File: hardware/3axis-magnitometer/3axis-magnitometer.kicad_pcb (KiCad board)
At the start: 2 copper layers, 94 x 94 mm, 84 parts, among them J1 Conn_01x40_Pin, J2 AVR-JTAG-10, J3 AVR-ISP-6, U1 PCF8563T, U10 SP3485CN, U11 LSM6DS3, U2 W25Q128JVS, U3 ATmega1284P-A, U4 QMC5883P, U5 AMS1117-3.3, U6 AMS1117-3.3, U7 74LVC2T45DC, U8 74LVC2T45DC, U9 SP3485CN, Y1 32.768кГц, Y2 8MHz

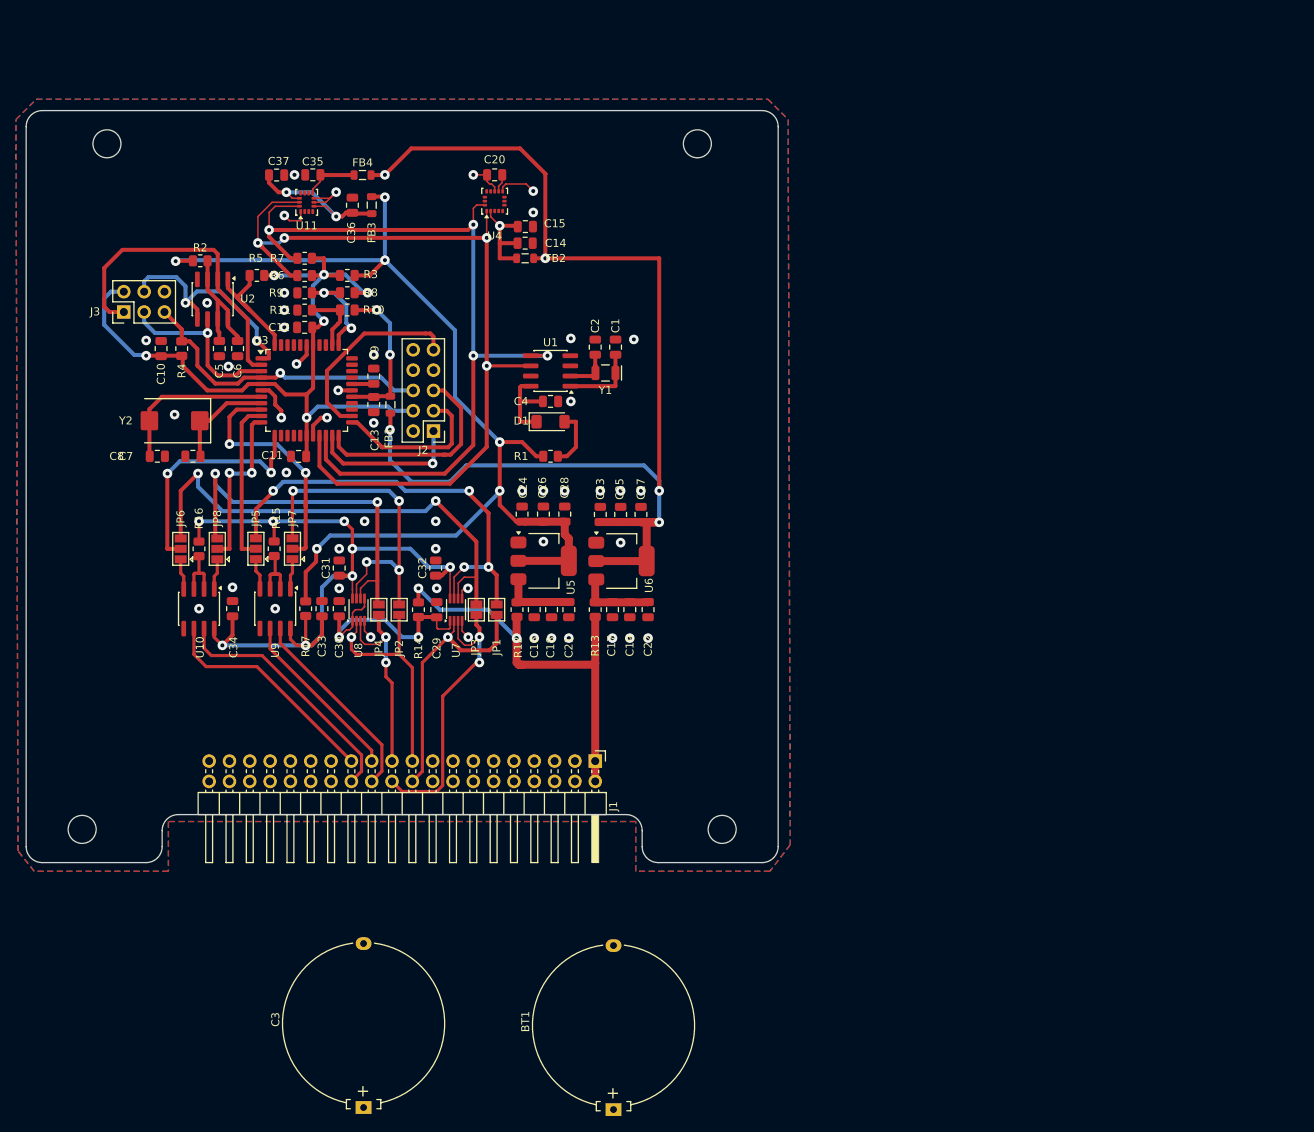
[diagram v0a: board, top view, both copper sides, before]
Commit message: Магнитометр правки
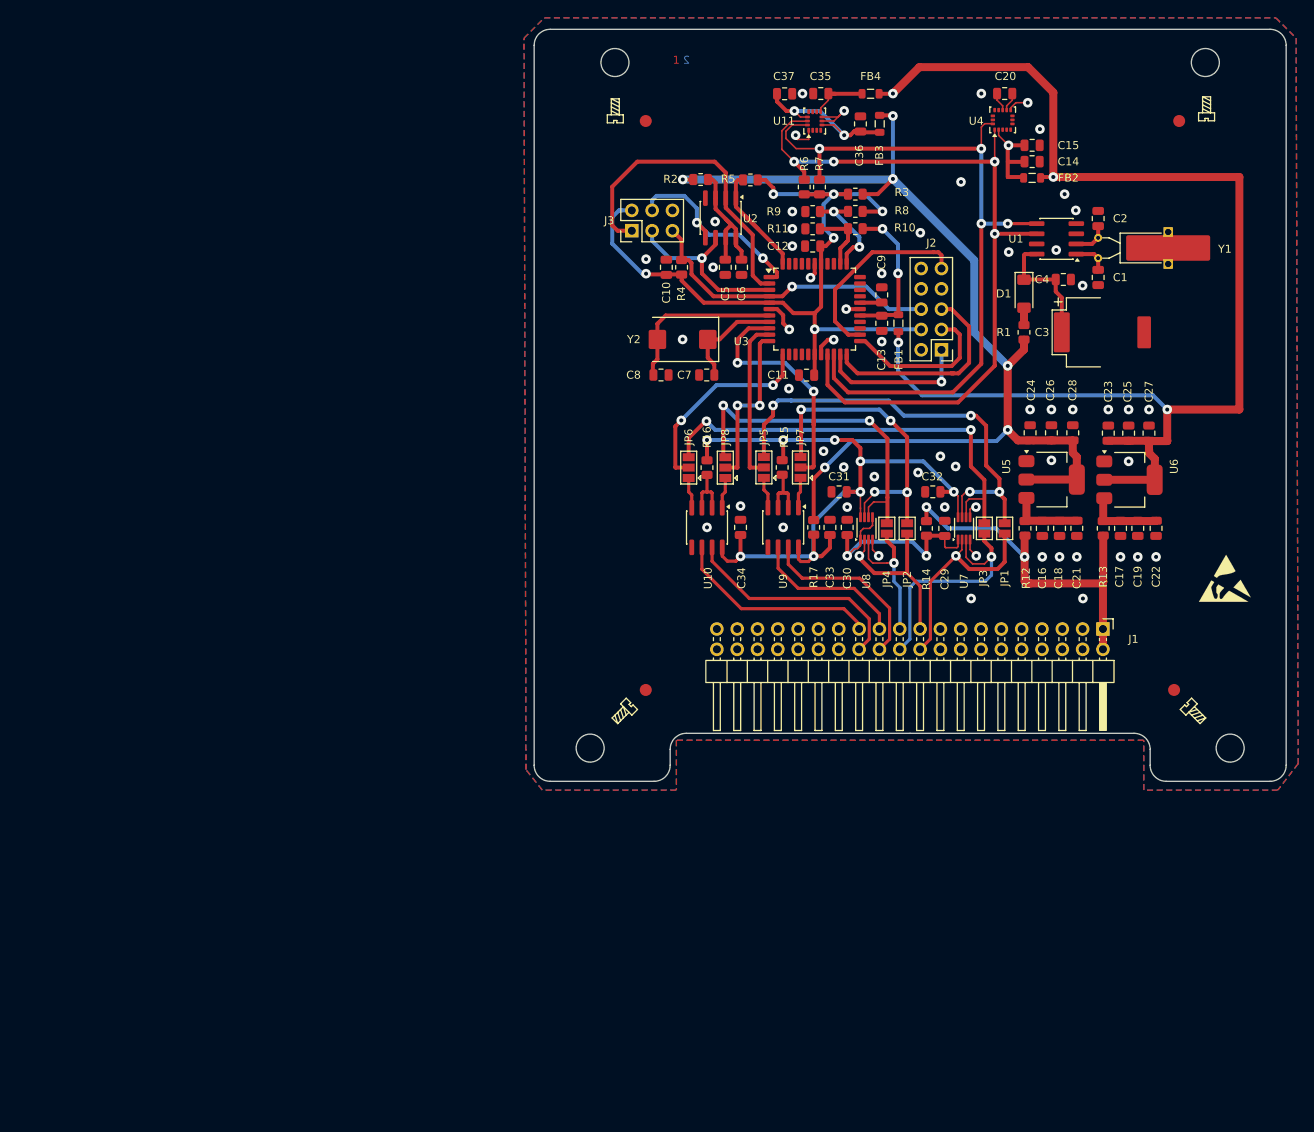
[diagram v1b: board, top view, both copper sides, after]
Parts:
- removed BT1: Battery_Cell, Battery:Battery_Panasonic_CR2032-HFN_Horizontal_CircularHoles
- added REF**: LayerMarker_2_3.81x2.54mm_TextH1mm_P1.27mm_BottomMirrored, Symbol:LayerMarker_2_3.81x2.54mm_TextH1mm_P1.27mm_BottomMirrored, F.Cu at (107.5, 43.8)
- added REF**: Screw_Generic_2.0x3.0mm_SilkScreen, Symbol:Screw_Generic_2.0x3.0mm_SilkScreen, F.Cu at (173.8, 48.7)
- added REF**: Fiducial_1.5mm_Mask3mm, Fiducial:Fiducial_1.5mm_Mask3mm, F.Cu at (103.7, 121.3)
- added REF**: Screw_Generic_2.0x3.0mm_SilkScreen, Symbol:Screw_Generic_2.0x3.0mm_SilkScreen, F.Cu at (172.3, 124.1)
- added REF**: Screw_Generic_2.0x3.0mm_SilkScreen, Symbol:Screw_Generic_2.0x3.0mm_SilkScreen, F.Cu at (100.9, 124.1)
- added REF**: Fiducial_1.5mm_Mask3mm, Fiducial:Fiducial_1.5mm_Mask3mm, F.Cu at (169.8, 121.3)
- added REF**: ESD-Logo_6.6x6mm_SilkScreen, Symbol:ESD-Logo_6.6x6mm_SilkScreen, F.Cu at (176.1, 107.3)
- added REF**: Screw_Generic_2.0x3.0mm_SilkScreen, Symbol:Screw_Generic_2.0x3.0mm_SilkScreen, F.Cu at (99.9, 48.9)
- added REF**: Fiducial_1.5mm_Mask3mm, Fiducial:Fiducial_1.5mm_Mask3mm, F.Cu at (170.4, 50.2)
- added REF**: Fiducial_1.5mm_Mask3mm, Fiducial:Fiducial_1.5mm_Mask3mm, F.Cu at (103.7, 50.2)
- C3: footprint Battery:Battery_Panasonic_CR2032-HFN_Horizontal_CircularHoles -> IONISTOR:DSK
- Y1: footprint Crystal:Crystal_SMD_EuroQuartz_EQ161-2Pin_3.2x1.5mm -> Crystal:Crystal_AT310_D3.0mm_L10.0mm_Horizontal_1EP_style2
- moved C3 133.9 mm to (160.9, 76.6), turned to 0 degrees
- moved C4 65.9 mm to (155.9, 70.0)
- moved J1 65.6 mm to (160.9, 113.7)
- moved U1 65.4 mm to (155.1, 64.9)
- moved C7 65.0 mm to (111.3, 81.9)
- moved R7 65.0 mm to (125.4, 58.4), turned to 90 degrees
- moved C2 64.9 mm to (160.3, 62.4)
- moved C20 64.6 mm to (148.6, 46.8)
- moved FB1 64.3 mm to (135.3, 75.5)
- moved C19 64.3 mm to (165.2, 101.1)
- moved C21 64.3 mm to (157.6, 101.1)
- moved C25 64.3 mm to (164.1, 89.2)
- moved C30 64.3 mm to (128.9, 101.0)
- moved C33 64.3 mm to (126.7, 101.0)
- moved C35 64.3 mm to (125.6, 46.8)
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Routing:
- net +3.3VA: track 147.5 -> 163.6 mm, vias 5 -> 4
- net /SDA: track 103.8 -> 94.5 mm
- net /SCL: track 107.2 -> 98.4 mm
- net /level_translator/RX0: track 28.9 -> 21.9 mm
- net /level_translator/RX1: track 25.1 -> 18.4 mm, vias 2 -> 1
- net Net-(D1-K): track 10.6 -> 17.1 mm
- net GND: track 39.6 -> 33.2 mm, vias 49 -> 57
- net +5V: track 53.4 -> 47.1 mm
- net /level_translator/TX0: track 32.9 -> 26.6 mm
- net Net-(U10-VCC): track 96.8 -> 91.1 mm
- net /level_translator/TX1: track 36.4 -> 30.8 mm, vias 2 -> 1
- net Net-(JP3-B): track 62.0 -> 56.3 mm
- net Net-(D1-A): track 7.34 -> 1.91 mm
- net Net-(U1-OSCI): track 9.66 -> 4.71 mm
- net /level_translator/UART_TX1: track 30.4 -> 25.9 mm
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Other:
- outline, holes or cut-outs redrawn

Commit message: Финальные правки трассировки
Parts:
- added C3: C_Polarized, IONISTOR:DSK, F.Cu at (170.4, 76.2)
- moved C23 8.60 mm to (176.1, 101.1)
- moved C18 8.60 mm to (171.7, 101.1)
- moved C20 8.60 mm to (173.8, 101.1)
- moved C24 8.60 mm to (170.1, 89.2)
- moved C26 8.60 mm to (172.7, 89.2)
- moved C28 8.60 mm to (175.2, 89.2)
- moved R13 8.60 mm to (169.5, 101.1)
- moved U6 8.60 mm to (172.8, 95.0)
- moved REF** 7.01 mm to (176.7, 114.3)
- moved C17 3.44 mm to (156.7, 101.1)
- moved C19 3.44 mm to (158.9, 101.1)
- moved C25 3.44 mm to (155.2, 89.2)
- moved C27 3.44 mm to (157.9, 89.2)
- moved C22 3.44 mm to (161.0, 101.1)
- moved C29 3.44 mm to (160.5, 89.2)
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- renumbered C9 to C10, C10 to C11, C11 to C12, C12 to C13, C13 to C14, C14 to C15, C15 to C16, C16 to C17, C17 to C18, C18 to C19, C19 to C20, C20 to C21, C21 to C22, C22 to C23, C23 to C24, C24 to C25, C25 to C26, C26 to C27, C27 to C28, C28 to C29, C29 to C30, C30 to C31, C31 to C32, C32 to C33, C33 to C34, C34 to C35, C35 to C36, C36 to C37, C37 to C38, C3 to C4, C4 to C5, C5 to C6, C6 to C7, C7 to C8, C8 to C9
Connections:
- Y1 pad 3: (no net) -> GND
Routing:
- net Net-(D1-K): track 17.1 -> 31.2 mm
- net +5V: track 47.1 -> 53.5 mm
- net +3.3VA: track 163.6 -> 158.8 mm
- net +3.3V: track 135.0 -> 137.1 mm
- net Net-(U10-VCC): track 91.1 -> 90.2 mm
- net GND: vias 57 -> 56

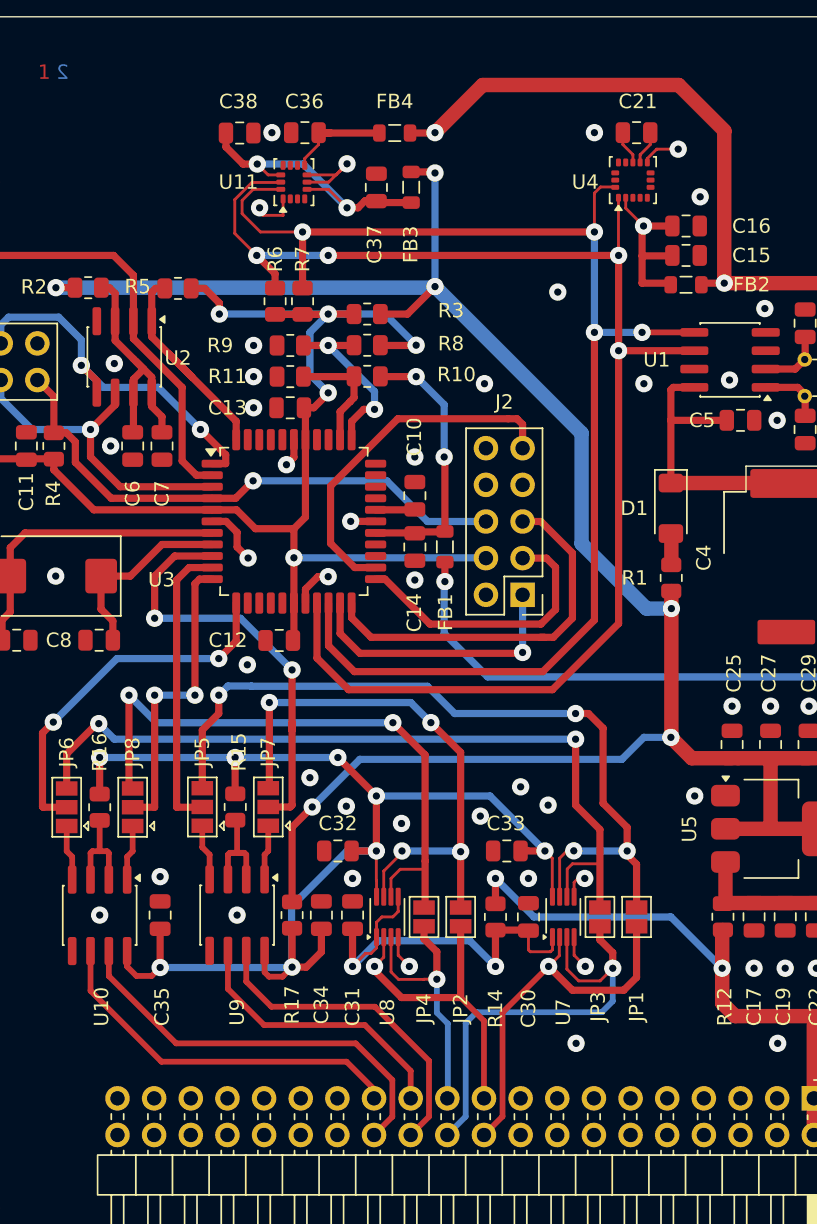
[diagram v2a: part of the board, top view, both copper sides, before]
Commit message: замена микросхемы преобразователя  уровня
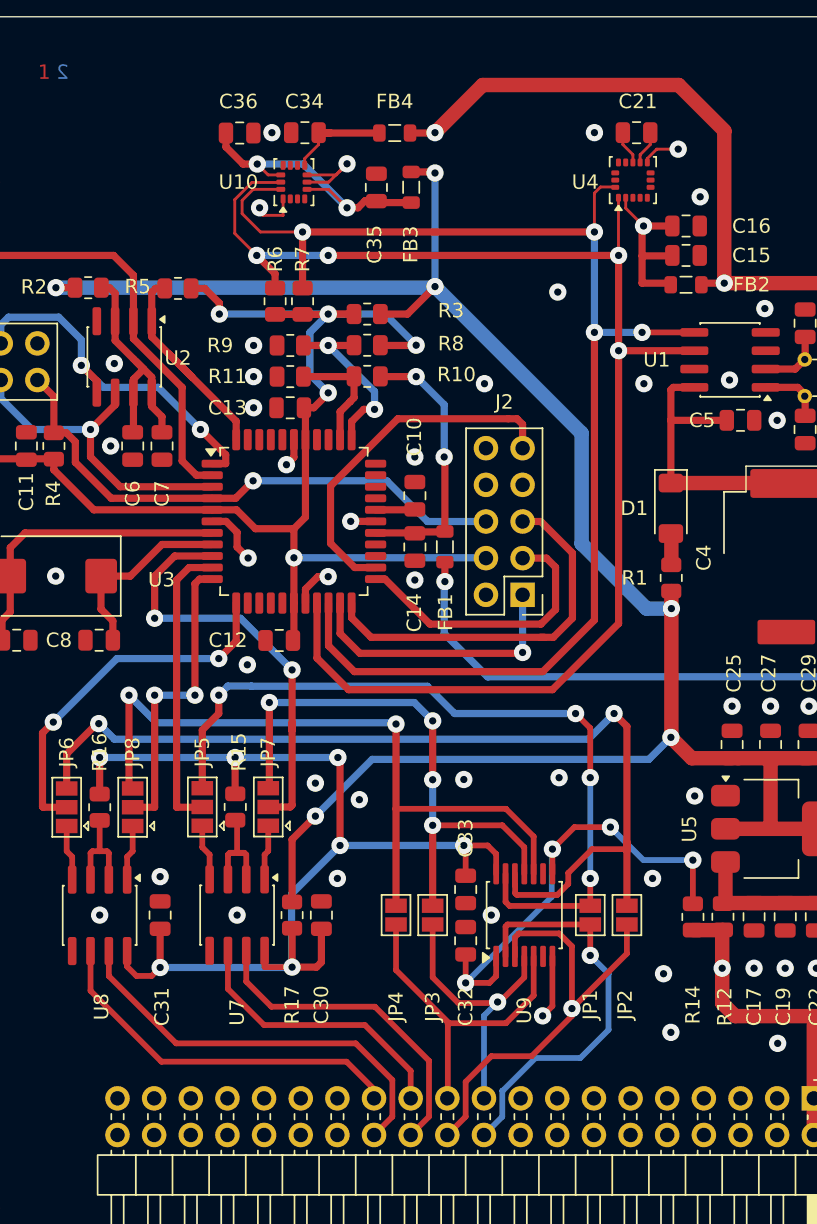
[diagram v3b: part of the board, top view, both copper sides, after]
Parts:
- removed the C30 at (141.1, 101.1)
- removed the C31 at (128.9, 101.0)
- removed the C33 at (139.6, 96.5)
- removed the U7 at (143.5, 101.1)
- removed the U8 at (131.3, 101.1)
- added C32: 0.22, Capacitor_SMD:C_0805_2012Metric, F.Cu at (136.7, 102.8)
- added U9: TXB0104PW, Package_SO:TSSOP-14_4.4x5mm_P0.65mm, F.Cu at (140.8, 101.0)
- moved R14 13.7 mm to (152.5, 101.1), turned to 90 degrees
- moved C33 9.25 mm to (136.7, 99.2), turned to -90 degrees
- moved JP1 3.21 mm to (145.4, 101.0)
- moved JP4 1.94 mm to (131.9, 101.0)
- moved JP3 1.94 mm to (134.5, 101.0)
- moved JP2 1.87 mm to (147.9, 101.0)
- renumbered C34 to C30, C35 to C31, C32 to C33, C36 to C34, C37 to C35, C38 to C36, JP3 to JP2, JP2 to JP3, U11 to U10, U9 to U7, U10 to U8
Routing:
- net +5V: track 53.5 -> 35.5 mm, vias 2 -> 1
- net Net-(U7-VCC): track 90.2 -> 78.2 mm, vias 8 -> 7
- net Net-(JP2-B): track 56.3 -> 68.0 mm
- net Net-(JP4-B): track 43.9 -> 51.4 mm
- net /level_translator/RX1: track 18.4 -> 23.1 mm, vias 1 -> 0
- net Net-(U9-OE): track 29.6 -> 33.5 mm, vias 2 -> 4
- net /level_translator/TX0: track 26.6 -> 28.5 mm
- net GND: track 33.2 -> 31.3 mm, vias 56 -> 54
- net /level_translator/RX0: track 21.9 -> 20.1 mm
- net Net-(JP1-B): track 56.2 -> 54.5 mm
- net /level_translator/TX1: track 30.8 -> 31.6 mm
- net +3.3V: track 137.1 -> 136.6 mm

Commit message: герберы и финальные правки
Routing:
- net GND: track 31.3 -> 33.7 mm, vias 54 -> 55
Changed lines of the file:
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@@
 		(pcbplotparams
 			(layerselection 0x00000000_00000000_55555555_5755f5ff)
-			(plot_on_all_layers_selection 0x00000000_00000000_00000000_00000000)
+			(plot_on_all_layers_selection 0x00000000_00000000_00000000_02000000)
 			(disableapertmacros no)
 			(usegerberextensions no)
@@
 			(sketchdnponfab yes)
 			(crossoutdnponfab yes)
-			(subtractmaskfromsilk no)
+			(subtractmaskfromsilk yes)
 			(outputformat 1)
 			(mirror no)
-			(drillshape 1)
+			(drillshape 0)
 			(scaleselection 1)
 			(outputdirectory "")
@@
 	)
 	(segment
+		(start 142.754 107.295)
+		(end 142.754 103.8525)
+		(width 0.4)
+		(layer "F.Cu")
+		(net 1)
+	)
+	(segment
 		(start 128.52 48.92)
 		(end 127.75 49.69)
@@
 	)
 	(segment
+		(start 140.296 109.499)
+		(end 140.55 109.499)
+		(width 0.4)
+		(layer "F.Cu")
+		(net 1)
+	)
+	(segment
 		(start 126.504675 77.531332)
 		(end 125.637 78.399007)
@@
 	)
 	(segment
+		(start 140.55 109.499)
+		(end 142.754 107.295)
+		(width 0.4)
+		(layer "F.Cu")
+		(net 1)
+	)
+	(segment
 		(start 149.983 47.904)
 		(end 149.332 48.555)
@@
 	)
 	(segment
-		(start 142.074 107.975)
-		(end 142.754 107.295)
-		(width 0.4)
-		(layer "F.Cu")
-		(net 1)
-	)
-	(segment
 		(start 127.213668 77.531332)
 		(end 126.504675 77.531332)
@@
 		(net 1)
 	)
-	(segment
-		(start 142.754 107.295)
-		(end 142.754 103.8525)
-		(width 0.4)
-		(layer "F.Cu")
-		(net 1)
-	)
 	(via
 		(at 122.459 51.968)
@@
 	)
 	(via
-		(at 143.217 91.465)
+		(at 143.217 91.592)
 		(size 1.2)
 		(drill 0.5)
@@
 	)
 	(via
-		(at 142.074 107.975)
+		(at 140.296 109.499)
 		(size 1.2)
 		(drill 0.5)
@@
 	)
 	(via
-		(at 129.374 92.989)
+		(at 130.136 92.608)
 		(size 1.2)
 		(drill 0.5)
@@
 	)
 	(via
-		(at 127.85 98.45)
+		(at 149.186 86.004)
+		(size 1.2)
+		(drill 0.5)
+		(layers "F.Cu" "B.Cu")
+		(free yes)
+		(net 1)
+	)
+	(via
+		(at 128.993 99.974)
 		(size 1.2)
 		(drill 0.5)
@@
 	)
 	(segment
-		(start 108.542 59.549)
-		(end 105.059 59.549)
+		(start 111.629 64.414)
+		(end 110.105 62.89)
 		(width 0.5)
 		(layer "B.Cu")
@@
 	)
 	(segment
-		(start 111.629 64.414)
-		(end 110.105 62.89)
+		(start 110.105 62.89)
+		(end 110.105 61.112)
 		(width 0.5)
 		(layer "B.Cu")
@@
 	)
 	(segment
-		(start 110.105 62.89)
-		(end 110.105 61.112)
+		(start 104.517 60.091)
+		(end 104.517 61.366)
 		(width 0.5)
 		(layer "B.Cu")
@@
 	)
 	(segment
-		(start 110.105 61.112)
-		(end 108.542 59.549)
+		(start 104.893 59.715)
+		(end 104.517 60.091)
 		(width 0.5)
 		(layer "B.Cu")
@@
 	)
 	(segment
-		(start 115.439 64.414)
-		(end 111.629 64.414)
+		(start 108.708 59.715)
+		(end 104.893 59.715)
 		(width 0.5)
 		(layer "B.Cu")
@@
 	)
 	(segment
-		(start 104.517 60.091)
-		(end 104.517 61.366)
+		(start 115.439 64.414)
+		(end 111.629 64.414)
 		(width 0.5)
 		(layer "B.Cu")
@@
 	)
 	(segment
-		(start 105.059 59.549)
-		(end 104.517 60.091)
+		(start 110.105 61.112)
+		(end 108.708 59.715)
 		(width 0.5)
 		(layer "B.Cu")
@@
 	)
 	(segment
-		(start 145.376 100.34)
-		(end 145.361 100.355)
-		(width 0.4)
-		(layer "F.Cu")
-		(net 57)
-	)
-	(segment
-		(start 145.361 100.355)
-		(end 139.788 100.355)
-		(width 0.4)
+		(start 118.487 88.163)
+		(end 118.487 91.816)
+		(width 0.5)
 		(layer "F.Cu")
 		(net 57)
 	)
 	(segment
-		(start 118.487 88.163)
-		(end 118.487 91.816)
+		(start 118.487 91.816)
+		(end 118.868 92.197)
 		(width 0.5)
 		(layer "F.Cu")
@@
 	)
 	(segment
-		(start 139.788 100.355)
-		(end 139.504 100.071)
+		(start 139.504 99.817)
+		(end 139.504 98.1275)
 		(width 0.4)
 		(layer "F.Cu")
@@
 	)
 	(segment
-		(start 118.487 91.816)
-		(end 118.868 92.197)
-		(width 0.5)
+		(start 145.361 100.355)
+		(end 140.042 100.355)
+		(width 0.4)
 		(layer "F.Cu")
 		(net 57)
 	)
 	(segment
-		(start 139.504 100.071)
-		(end 139.504 98.1275)
+		(start 140.042 100.355)
+		(end 139.504 99.817)
 		(width 0.4)
 		(layer "F.Cu")
@@
 		(net 57)
 	)
+	(segment
+		(start 145.376 100.34)
+		(end 145.361 100.355)
+		(width 0.4)
+		(layer "F.Cu")
+		(net 57)
+	)
 	(via
 		(at 145.376 98.45)
@@
 	)
 	(segment
-		(start 121.881 85.115)
-		(end 120.265 85.115)
-		(width 0.5)
-		(layer "B.Cu")
-		(net 57)
-	)
-	(segment
 		(start 134.0905 85.1325)
-		(end 121.8985 85.1325)
+		(end 120.2475 85.1325)
 		(width 0.5)
 		(layer "B.Cu")
@@
 	)
 	(segment
-		(start 145.376 98.45)
-		(end 145.376 91.465)
-		(width 0.4)
-		(layer "B.Cu")
-		(net 57)
-	)
-	(segment
 		(start 144.36 87.02)
 		(end 135.978 87.02)
@@
 	)
 	(segment
-		(start 120.265 85.115)
-		(end 119.63 85.75)
-		(width 0.5)
+		(start 145.376 98.45)
+		(end 145.376 91.465)
+		(width 0.4)
 		(layer "B.Cu")
 		(net 57)
 	)
 	(segment
-		(start 121.8985 85.1325)
-		(end 121.881 85.115)
+		(start 120.2475 85.1325)
+		(end 119.63 85.75)
 		(width 0.5)
 		(layer "B.Cu")
@@
 	)
 	(segment
-		(start 147.916 101.894)
-		(end 148.17 101.64)
-		(width 0.4)
-		(layer "F.Cu")
-		(net 59)
-	)
-	(segment
 		(start 136.74 114.96)
 		(end 135.47 116.23)
@@
 	)
 	(segment
-		(start 140.154 102.529)
-		(end 140.154 103.8525)
+		(start 140.804 110.769)
+		(end 138.518 110.769)
 		(width 0.4)
 		(layer "F.Cu")
@@
 	)
 	(segment
-		(start 147.916 103.657)
-		(end 147.916 101.894)
+		(start 147.916 101.894)
+		(end 148.17 101.64)
 		(width 0.4)
 		(layer "F.Cu")
@@
 	)
 	(segment
-		(start 144.106 107.975)
-		(end 141.312 110.769)
+		(start 140.154 102.529)
+		(end 140.154 103.8525)
 		(width 0.4)
 		(layer "F.Cu")
@@
 	)
 	(segment
-		(start 140.423 102.26)
-		(end 140.154 102.529)
+		(start 136.74 112.547)
+		(end 136.74 114.96)
 		(width 0.4)
 		(layer "F.Cu")
@@
 	)
 	(segment
-		(start 136.74 112.547)
-		(end 136.74 114.96)
+		(start 147.916 103.657)
+		(end 147.916 101.894)
 		(width 0.4)
 		(layer "F.Cu")
@@
 	)
 	(segment
-		(start 141.312 110.769)
-		(end 138.518 110.769)
+		(start 140.423 102.26)
+		(end 140.154 102.529)
 		(width 0.4)
 		(layer "F.Cu")
@@
 	)
 	(segment
-		(start 143.217 102.26)
-		(end 140.423 102.26)
+		(start 144.106 107.467)
+		(end 140.804 110.769)
 		(width 0.4)
 		(layer "F.Cu")
@@
 	)
 	(segment
-		(start 144.106 107.467)
-		(end 144.106 107.975)
+		(start 143.217 102.26)
+		(end 140.423 102.26)
 		(width 0.4)
 		(layer "F.Cu")
@@
 	)
 	(segment
-		(start 139.646 101.64)
-		(end 139.504 101.782)
+		(start 139.504 102.021)
+		(end 139.504 103.8525)
 		(width 0.4)
 		(layer "F.Cu")
@@
 	)
 	(segment
-		(start 139.504 101.782)
-		(end 139.504 103.8525)
+		(start 145.376 101.64)
+		(end 139.885 101.64)
 		(width 0.4)
 		(layer "F.Cu")
@@
 	)
 	(segment
-		(start 145.376 101.64)
-		(end 139.646 101.64)
+		(start 139.885 101.64)
+		(end 139.504 102.021)
 		(width 0.4)
 		(layer "F.Cu")
